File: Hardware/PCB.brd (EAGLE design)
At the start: 170.6 x 111.2 mm, 103 parts, among them IC1 BD5229G-TR, IC4 XC6220A331MR-G, J1 FH34SRJ-24S-0.5SH_99_, J3 QWIIC_RIGHT_ANGLE, J4 112A-TAAR-R03_ATTEND, Q1 20V/4.2A/52mΩ/1.4W, Q2 20V/4.2A/52mΩ/1.4W, Q3 SI1308EDL-T1-GE3, U1 W25Q512JVEIQ, U2 ESP32-C6-WROOM-1-N8, U3 DS3231SN#, U4 MAX17048G+T10

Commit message: Fix #2
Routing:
- net SCK: track 177.5 -> 179.1 mm
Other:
- outline, holes or cut-outs redrawn
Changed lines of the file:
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@@
 <board>
 <plain>
-<wire x1="0.9" y1="111.2" x2="0.5" y2="0" width="0.1524" layer="20"/>
 <wire x1="170.7" y1="0" x2="171.1" y2="67.2" width="0.1524" layer="20"/>
 <wire x1="171.1" y1="67.2" x2="93.1" y2="67.2" width="0.1524" layer="20"/>
@@
 <wire x1="94.28133125" y1="10" x2="94.28133125" y2="0" width="0.1524" layer="20"/>
 <wire x1="94.28133125" y1="0" x2="170.7" y2="0" width="0.1524" layer="20"/>
+<wire x1="0.9" y1="111.2" x2="0.9" y2="63.8" width="0.1524" layer="20"/>
+<wire x1="0.9" y1="63.8" x2="7.2" y2="63.8" width="0.1524" layer="20"/>
+<wire x1="7.2" y1="63.8" x2="7.2" y2="43.5" width="0.1524" layer="20"/>
+<wire x1="7.2" y1="43.5" x2="0.5" y2="43.5" width="0.1524" layer="20"/>
+<wire x1="0.5" y1="43.5" x2="0.5" y2="0" width="0.1524" layer="20"/>
 </plain>
 <attributes>
@@
 <wire x1="5.1245" y1="90.23275" x2="5.88625" y2="90.23275" width="0.15" layer="1"/>
 <wire x1="4.77825" y1="89.8865" x2="5.1245" y2="90.23275" width="0.15" layer="1"/>
-<wire x1="4.77825" y1="52.56075" x2="4.77825" y2="89.8865" width="0.15" layer="16"/>
-<wire x1="14.75025" y1="42.58875" x2="4.77825" y2="52.56075" width="0.15" layer="16"/>
 <wire x1="5.88625" y1="90.23275" x2="5.8980125" y2="90.2634625" width="0.15" layer="1"/>
-<wire x1="14.75025" y1="42.58875" x2="14.75025" y2="42.5195" width="0.15" layer="16"/>
+<wire x1="14.75025" y1="42.5195" x2="14.75025" y2="42.58875" width="0.15" layer="16"/>
 <wire x1="33.72475" y1="48.54425" x2="33.24" y2="48.54425" width="0.15" layer="1"/>
 <wire x1="33.24" y1="48.54425" x2="32.61675" y2="48.54425" width="0.15" layer="1"/>
@@
 <via x="33.17075" y="46.46675" extent="1-16" drill="0.3">
 </via>
+<wire x1="7.5512" y1="64.1512" x2="4.77825" y2="64.1512" width="0.15" layer="16"/>
+<wire x1="4.77825" y1="64.1512" x2="4.77825" y2="89.8865" width="0.15" layer="16"/>
+<wire x1="14.75025" y1="42.58875" x2="7.5512" y2="49.7878" width="0.15" layer="16"/>
+<wire x1="7.5512" y1="49.7878" x2="7.5512" y2="64.1512" width="0.15" layer="16"/>
 </signal>
 <signal name="MISO">

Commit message: Fix #12
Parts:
- removed TP10, TP11, TP5: TPTP20R, DeskAssistant v19 v1:TP20R
- added TP_EPD_CS, TP_EPD_DC, TP_GND: TPTP20R, DeskAssistant v19 v1:TP20R
- renumbered TP1 to TP_TX, TP12 to TP_EPD_RST, TP13 to TP_EPD_3V3_C, TP14 to TP_VBUS, TP15 to TP_INT_RTC, TP16 to TP_3V3, TP17 to TP_EPD_3V3, TP2 to TP_RX, TP3 to TP_VBAT, TP4 to TP_GND1, TP6 to TP_MISO, TP7 to TP_MOSI, TP8 to TP_SCK, TP9 to TP_EPD_BUSY
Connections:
- net EPD_CS: now also TP_EPD_CS.TP; no longer TP10.TP
- net EPD_DC: now also TP_EPD_DC.TP; no longer TP11.TP
- net GND: now also TP_GND.TP; no longer TP5.TP
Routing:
- net GND: track 715.9 -> 709.0 mm
- net EPD_DC: track 144.1 -> 148.1 mm
- net EPD_CS: track 130.5 -> 132.4 mm

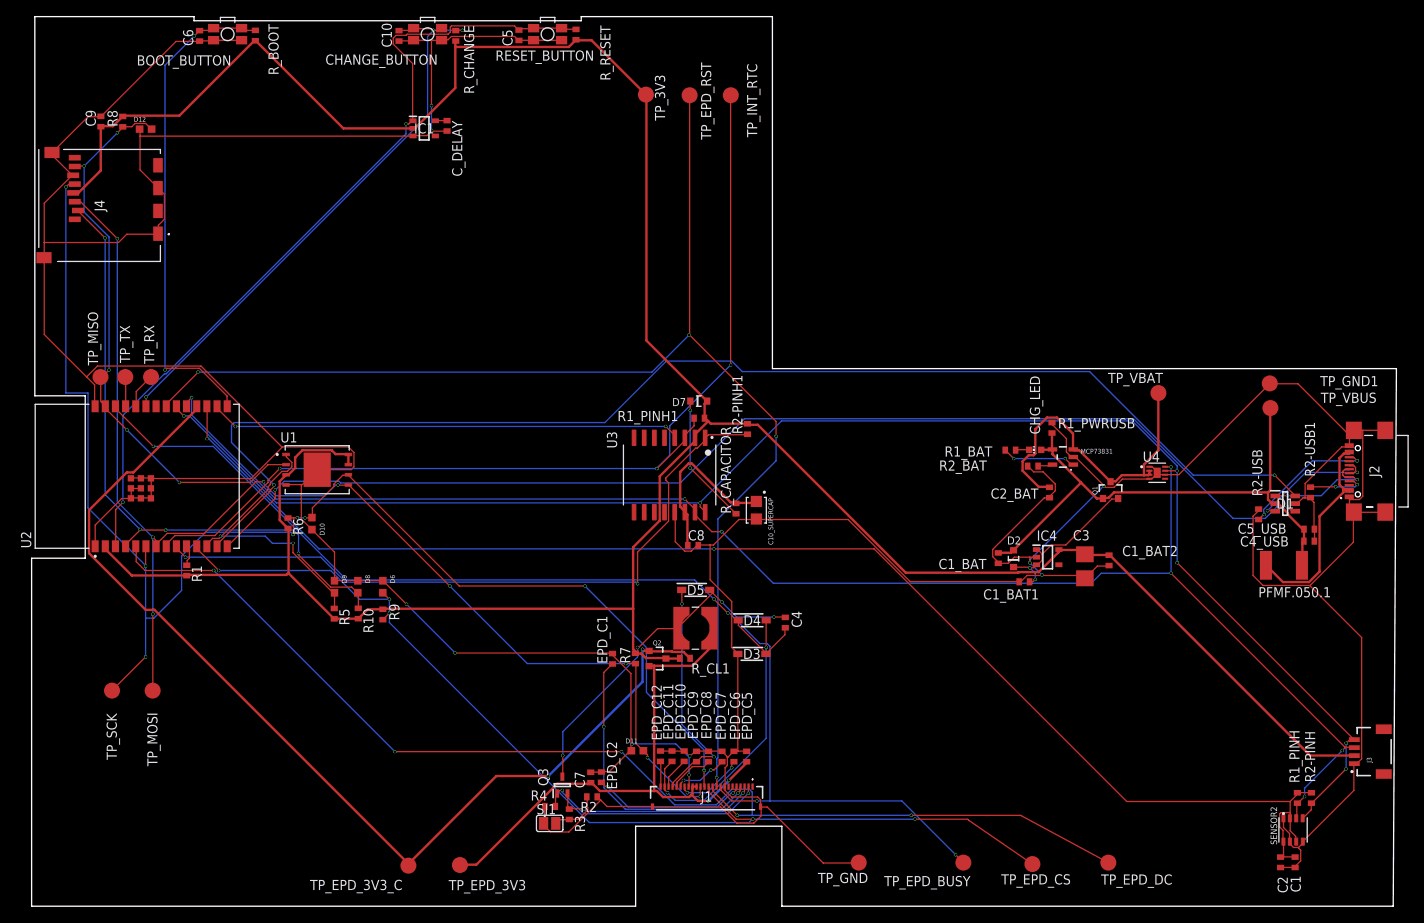
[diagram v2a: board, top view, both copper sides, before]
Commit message: Fix #13
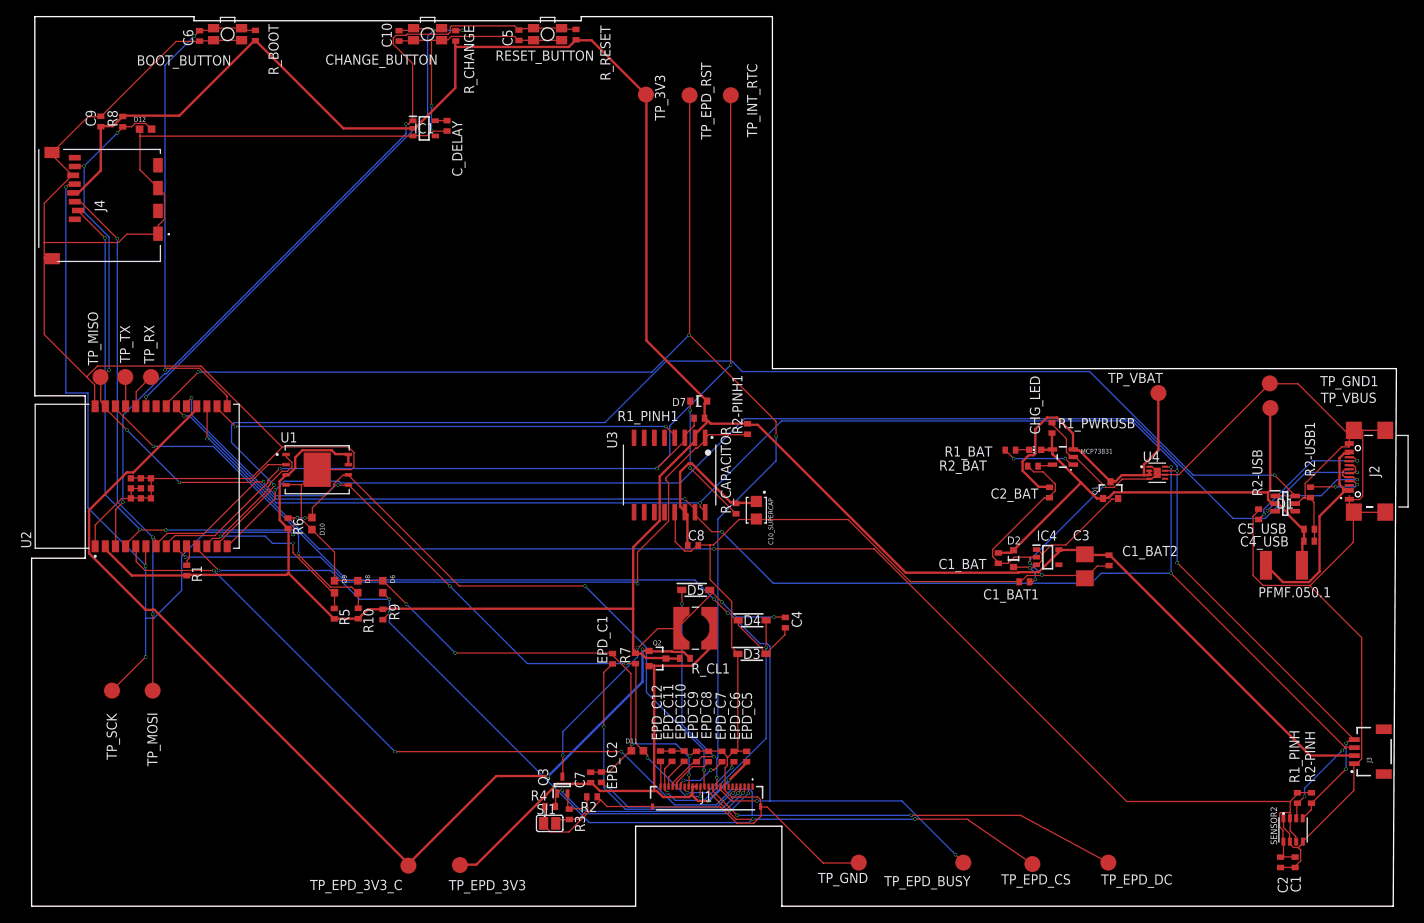
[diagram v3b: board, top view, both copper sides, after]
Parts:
- J2: value (none) -> SAMACSYS_PARTS_USB4110-GF-A
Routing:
- net GND: track 709.0 -> 712.6 mm
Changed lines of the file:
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@@
 <attribute name="VALUE" x="84.87" y="13.7" size="1.27" layer="27" align="center"/>
 </element>
-<element name="J2" library="DeskAssistant v19 v1" library_urn="urn:adsk.wipprod:fs.file:vf.H5hDozG6QPetQDMEzkF4lg" package="SAMACSYS_PARTS_USB4110GFA" value="" x="168.88353125" y="54.37188125" smashed="yes" rot="R90">
+<element name="J2" library="DeskAssistant v19 v1" library_urn="urn:adsk.wipprod:fs.file:vf.H5hDozG6QPetQDMEzkF4lg" package="SAMACSYS_PARTS_USB4110GFA" value="SAMACSYS_PARTS_USB4110-GF-A" x="168.88353125" y="54.37188125" smashed="yes" rot="R90">
 <attribute name="ARROW_PART_NUMBER" value="" x="204.44353125" y="87.39188125" size="1.778" layer="27" rot="R90" display="off"/>
 <attribute name="ARROW_PRICE-STOCK" value="" x="204.44353125" y="87.39188125" size="1.778" layer="27" rot="R90" display="off"/>
@@
 <wire x1="16.343" y1="85.10825" x2="16.343" y2="84.0695" width="0.15" layer="1"/>
 <wire x1="17.10475" y1="85.87" x2="16.343" y2="85.10825" width="0.15" layer="1"/>
-<wire x1="17.10475" y1="88.98625" x2="17.10475" y2="85.87" width="0.15" layer="1"/>
+<wire x1="17.10475" y1="85.87" x2="17.10475" y2="88.98625" width="0.15" layer="1"/>
 <wire x1="16.343" y1="89.748" x2="17.10475" y2="88.98625" width="0.15" layer="1"/>
 <wire x1="16.343" y1="84.0695" x2="16.2980125" y2="84.0634625" width="0.15" layer="1"/>
@@
 <wire x1="2.0775" y1="81.0225" x2="2.0775" y2="71.466" width="0.15" layer="1"/>
 <wire x1="8.37925" y1="62.53275" x2="8.44" y2="62.49" width="0.15" layer="1"/>
-<wire x1="2.0775" y1="81.0225" x2="2.0480125" y2="81.0634625" width="0.15" layer="1"/>
+<wire x1="2.0775" y1="81.0225" x2="3.08433125" y2="80.939003125" width="0.15" layer="1"/>
 <wire x1="23.1295" y1="108.1685" x2="21.53675" y2="108.1685" width="0.15" layer="1"/>
 <wire x1="23.19875" y1="108.23775" x2="23.1295" y2="108.1685" width="0.15" layer="1"/>
@@
 <wire x1="3.11625" y1="94.24925" x2="7.54825" y2="98.68125" width="0.15" layer="1"/>
 <wire x1="9.141" y1="98.68125" x2="9.16" y2="98.74" width="0.15" layer="1"/>
-<wire x1="3.11625" y1="94.24925" x2="3.0480125" y2="94.2134625" width="0.15" layer="1"/>
-<wire x1="5.54" y1="91.41" x2="5.6785" y2="91.41" width="0.15" layer="1"/>
-<wire x1="3.11625" y1="93.83375" x2="5.54" y2="91.41" width="0.15" layer="1"/>
-<wire x1="3.11625" y1="94.18" x2="3.11625" y2="93.83375" width="0.15" layer="1"/>
-<wire x1="5.6785" y1="91.41" x2="5.6980125" y2="91.3634625" width="0.15" layer="1"/>
+<wire x1="3.0480125" y1="94.2134625" x2="3.11625" y2="94.24925" width="0.15" layer="1"/>
+<wire x1="5.6785" y1="91.41" x2="5.54" y2="91.41" width="0.15" layer="1"/>
+<wire x1="5.54" y1="91.41" x2="3.11625" y2="93.83375" width="0.15" layer="1"/>
+<wire x1="3.11625" y1="93.83375" x2="3.11625" y2="94.18" width="0.15" layer="1"/>
+<wire x1="5.6980125" y1="91.3634625" x2="5.6785" y2="91.41" width="0.15" layer="1"/>
 <wire x1="3.11625" y1="94.18" x2="3.0480125" y2="94.2134625" width="0.15" layer="1"/>
 <wire x1="18.559" y1="108.09925" x2="21.4675" y2="108.09925" width="0.15" layer="1"/>
@@
 <wire x1="2.0775" y1="87.87825" x2="2.0775" y2="82.9615" width="0.15" layer="1"/>
 <wire x1="2.0775" y1="82.9615" x2="2.0775" y2="81.09175" width="0.15" layer="1"/>
-<wire x1="5.54" y1="91.34075" x2="2.0775" y2="87.87825" width="0.15" layer="1"/>
-<wire x1="2.0775" y1="81.09175" x2="2.0480125" y2="81.0634625" width="0.15" layer="1"/>
+<wire x1="2.0775" y1="87.87825" x2="5.54" y2="91.34075" width="0.15" layer="1"/>
+<wire x1="3.08433125" y1="80.939003125" x2="2.0775" y2="81.09175" width="0.15" layer="1"/>
 <wire x1="5.54" y1="91.34075" x2="5.6980125" y2="91.3634625" width="0.15" layer="1"/>
 <wire x1="21.67525" y1="67.51875" x2="31.820375" y2="57.373625" width="0.15" layer="1"/>
@@
 <wire x1="158.8595" y1="7.27125" x2="158.8595" y2="7.3405" width="0.15" layer="1"/>
 <wire x1="165.2305" y1="51.31425" x2="165.2305" y2="51.03725" width="0.15" layer="1"/>
-<wire x1="165.2305" y1="51.03725" x2="165.20553125" y2="51.02188125" width="0.15" layer="1"/>
-<wire x1="165.2305" y1="51.31425" x2="165.20553125" y2="51.32188125" width="0.15" layer="1"/>
+<wire x1="165.2305" y1="51.03725" x2="165.22585" y2="50.719621875" width="0.15" layer="1"/>
+<wire x1="165.22585" y1="51.019621875" x2="165.2305" y2="51.31425" width="0.15" layer="1"/>
 <wire x1="153.8735" y1="49.4445" x2="153.8735" y2="49.583" width="0.15" layer="1"/>
 <wire x1="153.181" y1="48.752" x2="153.8735" y2="49.4445" width="0.15" layer="1"/>
@@
 <wire x1="165.2305" y1="50.8295" x2="165.2305" y2="50.968" width="0.15" layer="1"/>
 <wire x1="165.71525" y1="49.306" x2="165.2305" y2="49.79075" width="0.15" layer="1"/>
-<wire x1="165.2305" y1="50.968" x2="165.20553125" y2="51.02188125" width="0.15" layer="1"/>
+<wire x1="165.22585" y1="50.719621875" x2="165.2305" y2="50.968" width="0.15" layer="1"/>
 <wire x1="165.71525" y1="49.306" x2="165.78053125" y2="49.26188125" width="0.15" layer="1"/>
 <wire x1="165.85375" y1="49.23675" x2="169.6625" y2="49.23675" width="0.15" layer="1"/>
@@
 <wire x1="160.7985" y1="47.15925" x2="160.85" y2="47.13" width="0.15" layer="1"/>
 <wire x1="160.31375" y1="50.968" x2="160.36" y2="51.08" width="0.15" layer="1"/>
-<wire x1="165.2305" y1="57.68525" x2="165.2305" y2="57.4775" width="0.15" layer="1"/>
-<wire x1="165.2305" y1="57.4775" x2="165.20553125" y2="57.42188125" width="0.15" layer="1"/>
-<wire x1="165.2305" y1="57.68525" x2="165.20553125" y2="57.72188125" width="0.15" layer="1"/>
+<wire x1="165.2305" y1="57.4775" x2="165.2305" y2="57.68525" width="0.15" layer="1"/>
+<wire x1="165.20553125" y1="57.6835" x2="165.2305" y2="57.4775" width="0.15" layer="1"/>
+<wire x1="165.2305" y1="57.68525" x2="165.20553125" y2="57.9835" width="0.15" layer="1"/>
 <wire x1="165.2305" y1="58.93175" x2="165.2305" y2="57.7545" width="0.15" layer="1"/>
 <wire x1="165.71525" y1="59.4165" x2="165.2305" y2="58.93175" width="0.15" layer="1"/>
-<wire x1="165.2305" y1="57.7545" x2="165.20553125" y2="57.72188125" width="0.15" layer="1"/>
+<wire x1="165.20553125" y1="57.9835" x2="165.2305" y2="57.7545" width="0.15" layer="1"/>
 <wire x1="165.71525" y1="59.4165" x2="165.78053125" y2="59.48188125" width="0.15" layer="1"/>
 <wire x1="158.79025" y1="65.30275" x2="155.32775" y2="65.30275" width="0.15" layer="1"/>
@@
 <wire x1="164.261" y1="57.40825" x2="159.6905" y2="52.83775" width="0.15" layer="1"/>
 <wire x1="165.16125" y1="57.40825" x2="164.261" y2="57.40825" width="0.15" layer="1"/>
-<wire x1="165.16125" y1="57.40825" x2="165.20553125" y2="57.42188125" width="0.15" layer="1"/>
+<wire x1="165.16125" y1="57.40825" x2="165.20553125" y2="57.6835" width="0.15" layer="1"/>
 <wire x1="143.9015" y1="53.94575" x2="142.2395" y2="53.94575" width="0.15" layer="1"/>
 <wire x1="155.2585" y1="65.30275" x2="143.9015" y2="53.94575" width="0.15" layer="1"/>
@@
 <wire x1="9.76425" y1="44.94325" x2="9.76425" y2="44.597" width="0.3" layer="1"/>
 <wire x1="19.87475" y1="41.34225" x2="19.89" y2="41.32" width="0.3" layer="1"/>
-<wire x1="9.76425" y1="44.94325" x2="9.71" y2="44.99" width="0.3" layer="1"/>
+<wire x1="9.71" y1="44.99" x2="9.76425" y2="44.94325" width="0.3" layer="1"/>
 <wire x1="41.273" y1="35.94075" x2="38.3645" y2="35.94075" width="0.3" layer="1"/>
 <wire x1="38.3645" y1="35.94075" x2="38.33" y2="35.92" width="0.3" layer="1"/>
